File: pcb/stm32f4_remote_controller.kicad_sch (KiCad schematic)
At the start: 19 parts, among them J1 Conn_01x04_Pin, SW1 SW_Push, U1 STM32F401CCU6, U2 OLED DISPLAY, Y1 8Mhz

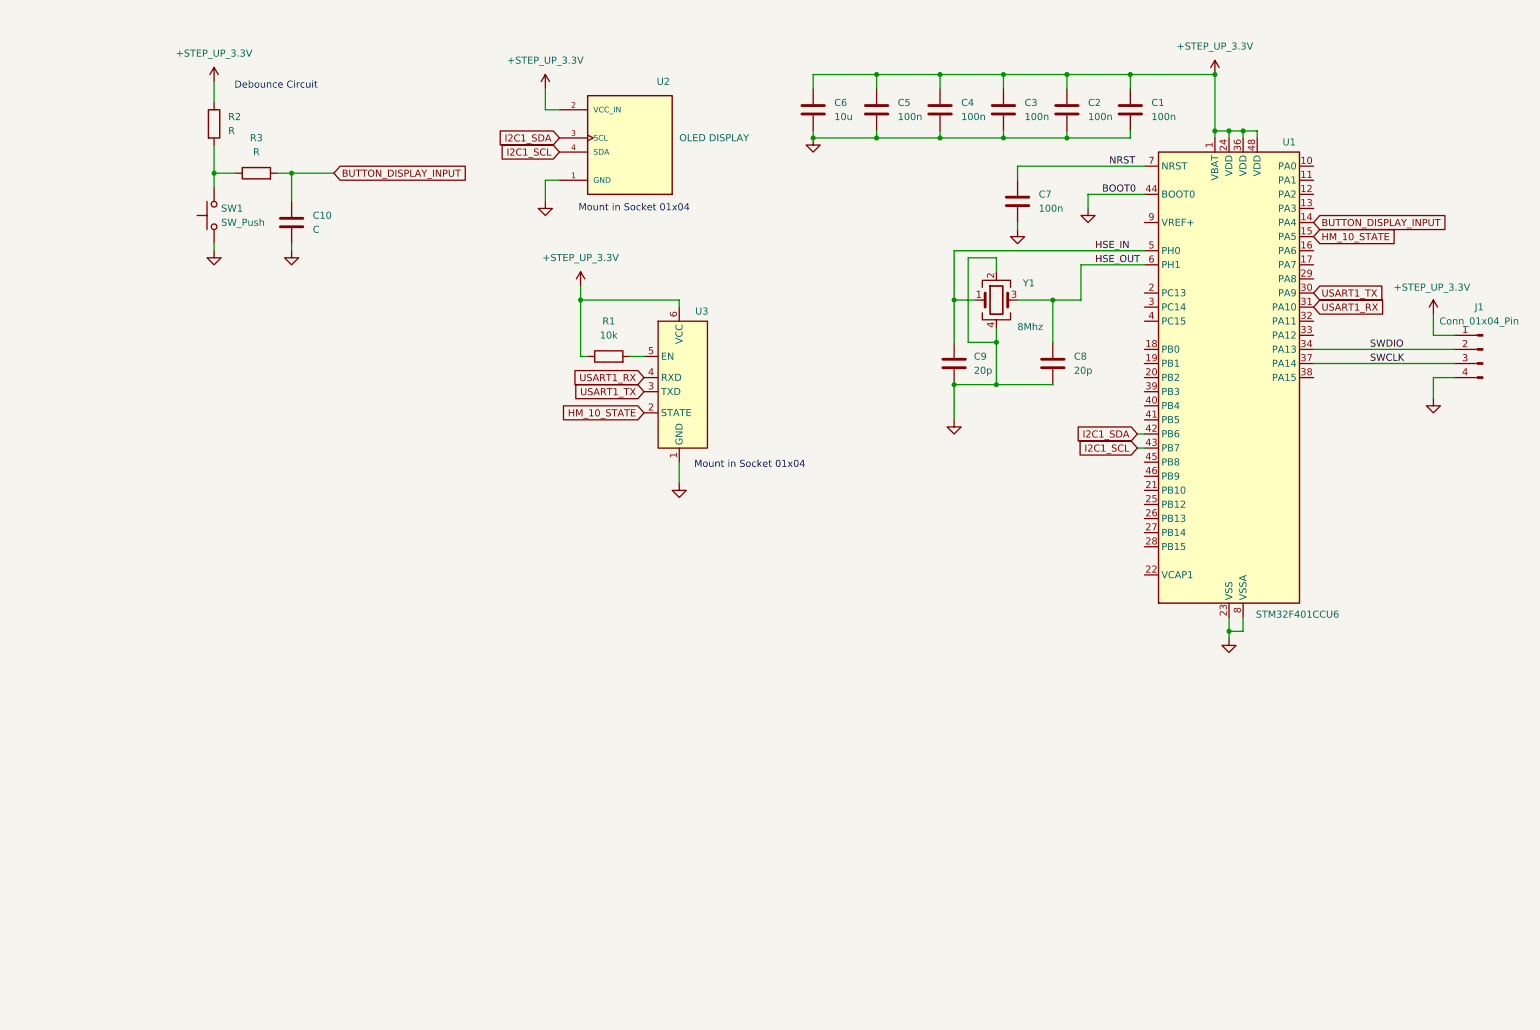
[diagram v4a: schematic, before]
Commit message: pcb: add analog joystick connection to adc
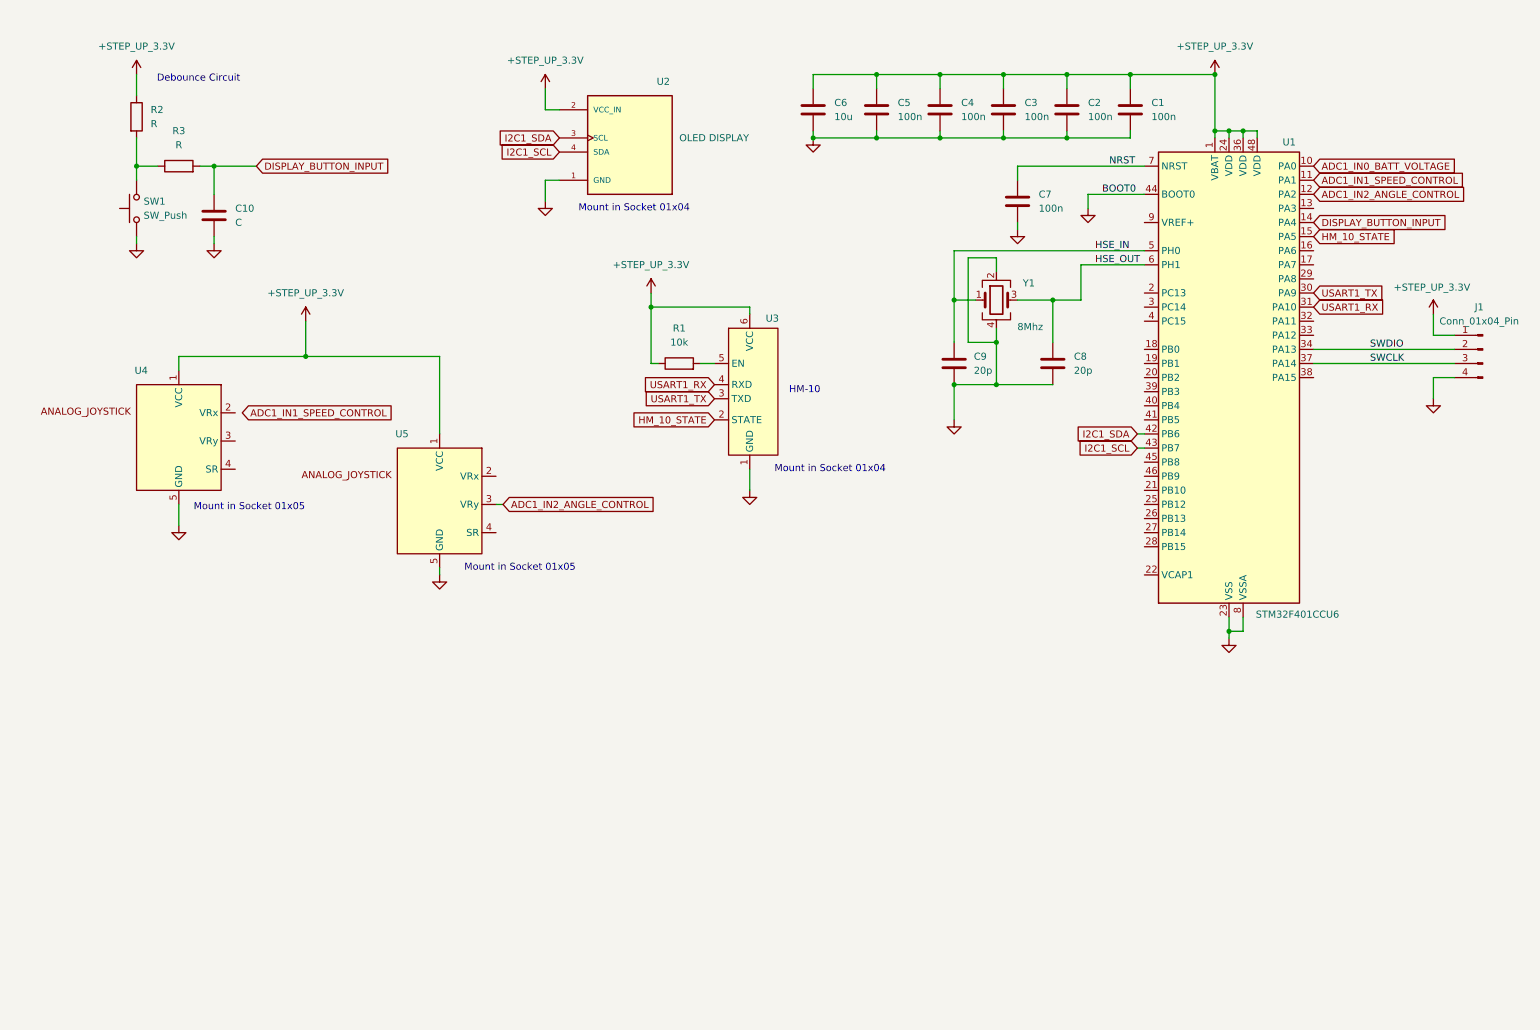
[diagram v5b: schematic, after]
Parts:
- added U4, U5: ~, symbol joystick:analog_joystick
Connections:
- net +STEP_UP_3.3V: now also U4.1 (VCC), U5.1 (VCC)
- net GND: now also U4.5 (GND), U5.5 (GND)
- net ADC1_IN0_BATT_VOLTAGE: now reaches U1.10 (PA0)
- net ADC1_IN1_SPEED_CONTROL: now reaches U1.11 (PA1)
- net ADC1_IN2_ANGLE_CONTROL: now reaches U1.12 (PA2)
- net ADC1_IN2_ANGLE_CONTROL: now also U5.3 (VRy)
- net BUTTON_DISPLAY_INPUT renamed DISPLAY_BUTTON_INPUT
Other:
- note added: "HM-10"
- note added: "Mount in Socket 01x05"
- moved on the sheet: C10, R1, R2, R3, SW1, U3

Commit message: pcb: add sections
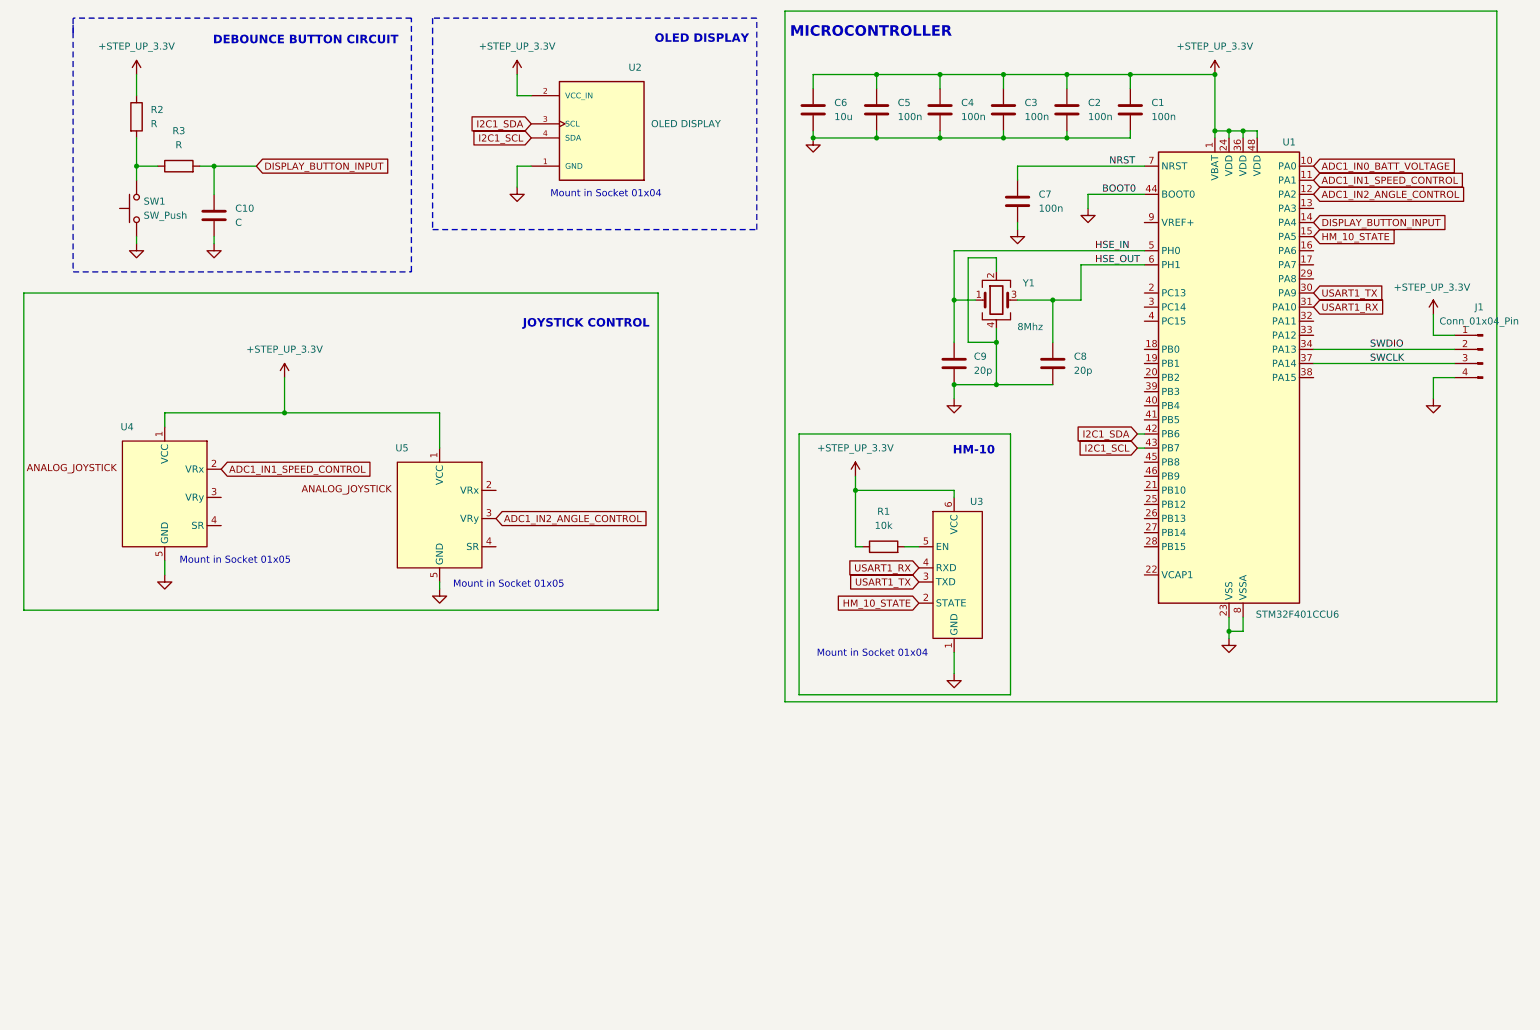
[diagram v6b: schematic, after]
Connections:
- net ADC1_IN1_SPEED_CONTROL: now also U4.2 (VRx)
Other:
- note added: "DEBOUNCE BUTTON CIRCUIT"
- note added: "JOYSTICK CONTROL"
- note added: "MICROCONTROLLER"
- note added: "OLED DISPLAY"
- note removed: "Debounce Circuit"
- moved on the sheet: R1, U2, U3, U4, U5

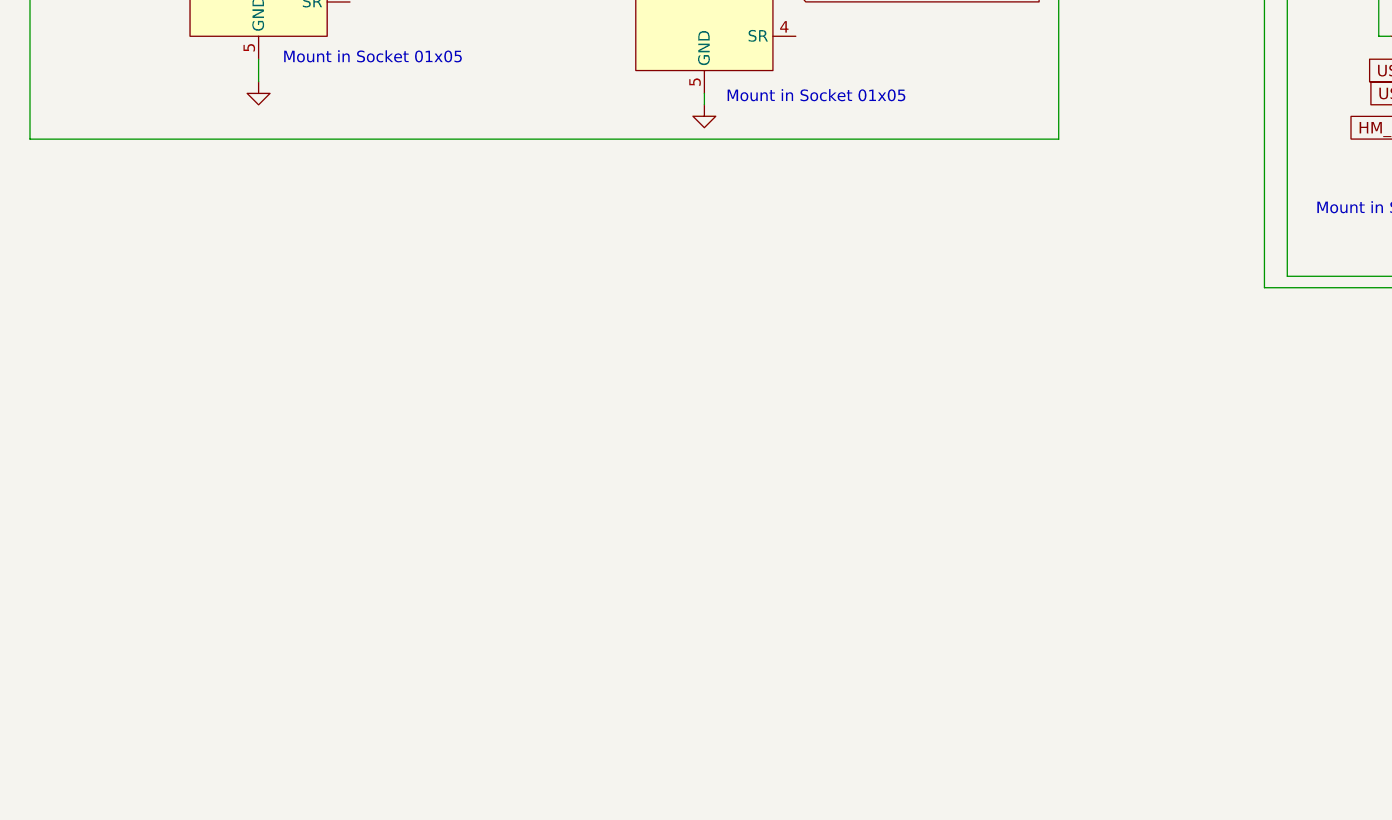
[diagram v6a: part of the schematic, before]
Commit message: pcb: add DC-DC STEP UP converter
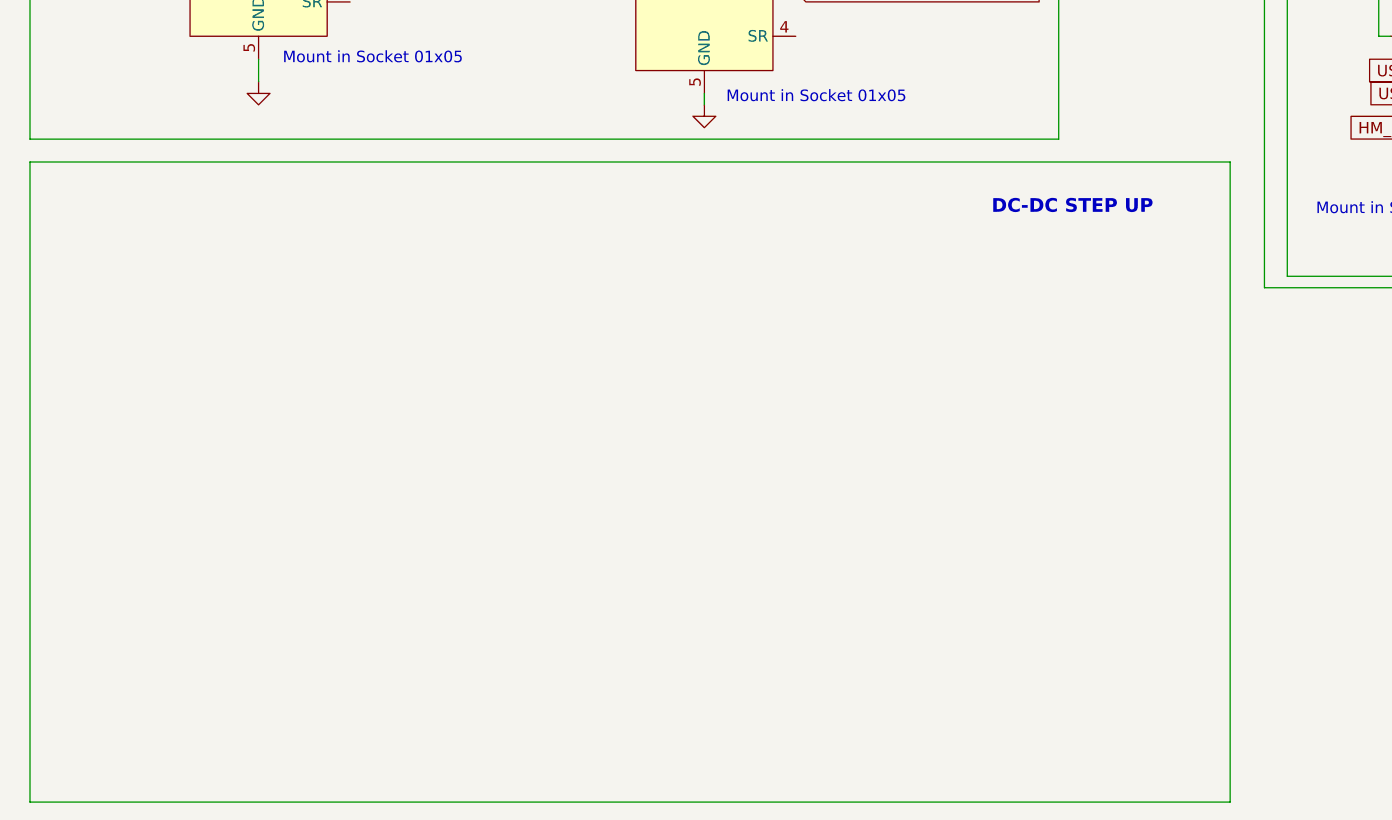
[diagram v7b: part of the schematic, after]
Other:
- note added: "DC-DC STEP UP"
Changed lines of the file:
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@@
+		)
+	)
+	(wire
+		(pts
+			(xy 15.24 195.58) (xy 148.59 195.58)
+		)
+		(stroke
+			(width 0)
+			(type dash)
+			(color 0 3 255 1)
 		)
 	)
@@
 	(wire
 		(pts
+			(xy 148.59 124.46) (xy 15.24 124.46)
+		)
+		(stroke
+			(width 0)
+			(type dash)
+			(color 0 3 255 1)
+		)
+	)
+	(wire
+		(pts
 			(xy 215.9 90.17) (xy 217.17 90.17)
 		)
@@
 	(wire
 		(pts
+			(xy 15.24 124.46) (xy 15.24 195.58)
+		)
+		(stroke
+			(width 0)
+			(type dash)
+			(color 0 3 255 1)
+		)
+	)
+	(wire
+		(pts
 			(xy 190.5 71.12) (xy 190.5 73.66)
 		)
@@
 			(width 0)
 			(type dash)
+		)
+	)
+	(wire
+		(pts
+			(xy 148.59 195.58) (xy 148.59 124.46)
+		)
+		(stroke
+			(width 0)
+			(type dash)
+			(color 0 3 255 1)
 		)
 	)
@@
 			)
 		)
+	)
+	(text "DC-DC STEP UP\n"
+		(exclude_from_sim no)
+		(at 131.064 129.54 0)
+		(effects
+			(font
+				(size 1.524 1.524)
+				(thickness 0.254)
+				(bold yes)
+			)
+		)

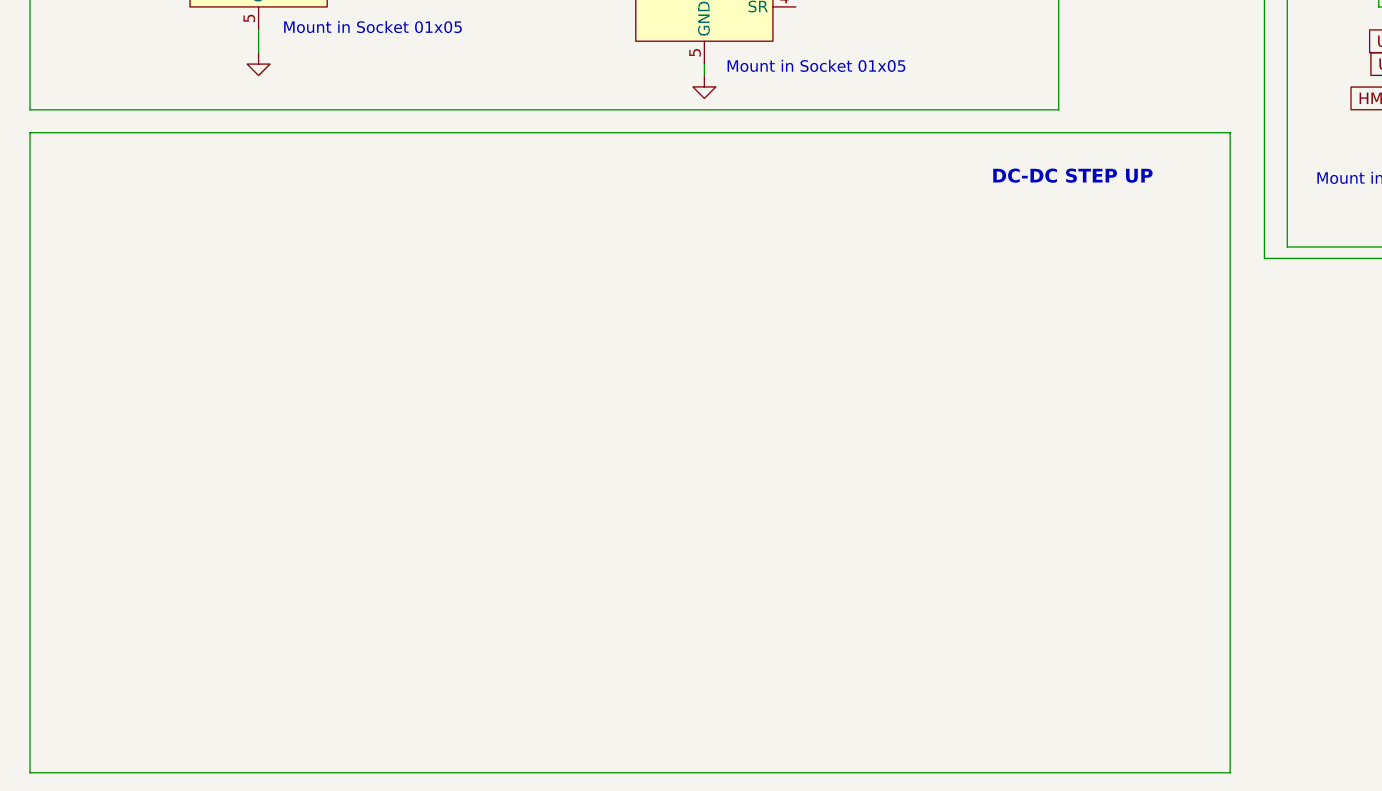
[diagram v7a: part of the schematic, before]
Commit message: pcb: add dc-dc-step-up sch
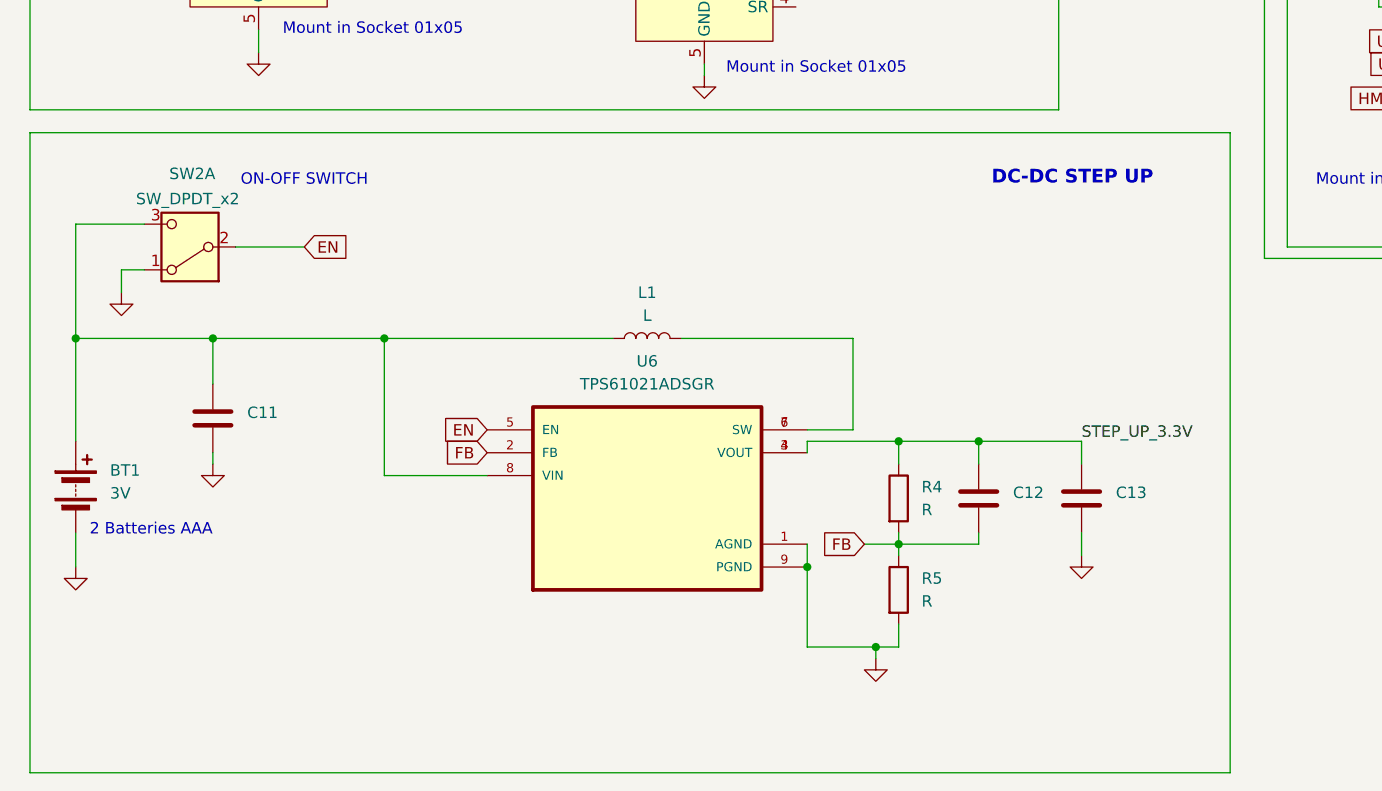
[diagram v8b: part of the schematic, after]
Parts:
- added BT1: 3V, symbol Device:Battery
- added C11, C12, C13: ~, symbol Device:C
- added L1: L, symbol Device:L
- added R4, R5: R, symbol Device:R
- added SW2: SW_DPDT_x2, symbol Switch:SW_DPDT_x2
- added U6: TPS61021ADSGR, TPS61021ADSGR:SON50P200X200X80-9N, symbol TPS61021ADSGR:TPS61021ADSGR
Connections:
- net GND: now also BT1.2 (-), C11.2, C13.2, R5.2, SW2.1 (A), U6.1 (AGND), U6.9 (PGND)
- new net: BT1.1 (+), C11.1, L1.1, SW2.3 (C), U6.8 (VIN)
- new net: L1.2, U6.6 (SW), U6.7 (SW)
- new net EN: SW2.2 (B), U6.5 (EN)
- new net FB: C12.2, R4.2, R5.1, U6.2 (FB)
- new net STEP_UP_3.3V: C12.1, C13.1, R4.1, U6.3 (VOUT), U6.4 (VOUT)
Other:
- note added: "2 Batteries AAA"
- note added: "ON-OFF SWITCH"
